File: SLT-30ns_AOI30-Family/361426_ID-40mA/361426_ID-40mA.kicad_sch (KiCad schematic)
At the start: 9 parts, among them T1 IBM_Transistor, T2 IBM_Transistor, T3 IBM_Transistor, T4 IBM_Transistor, U1 12-Pin_SLx_Can

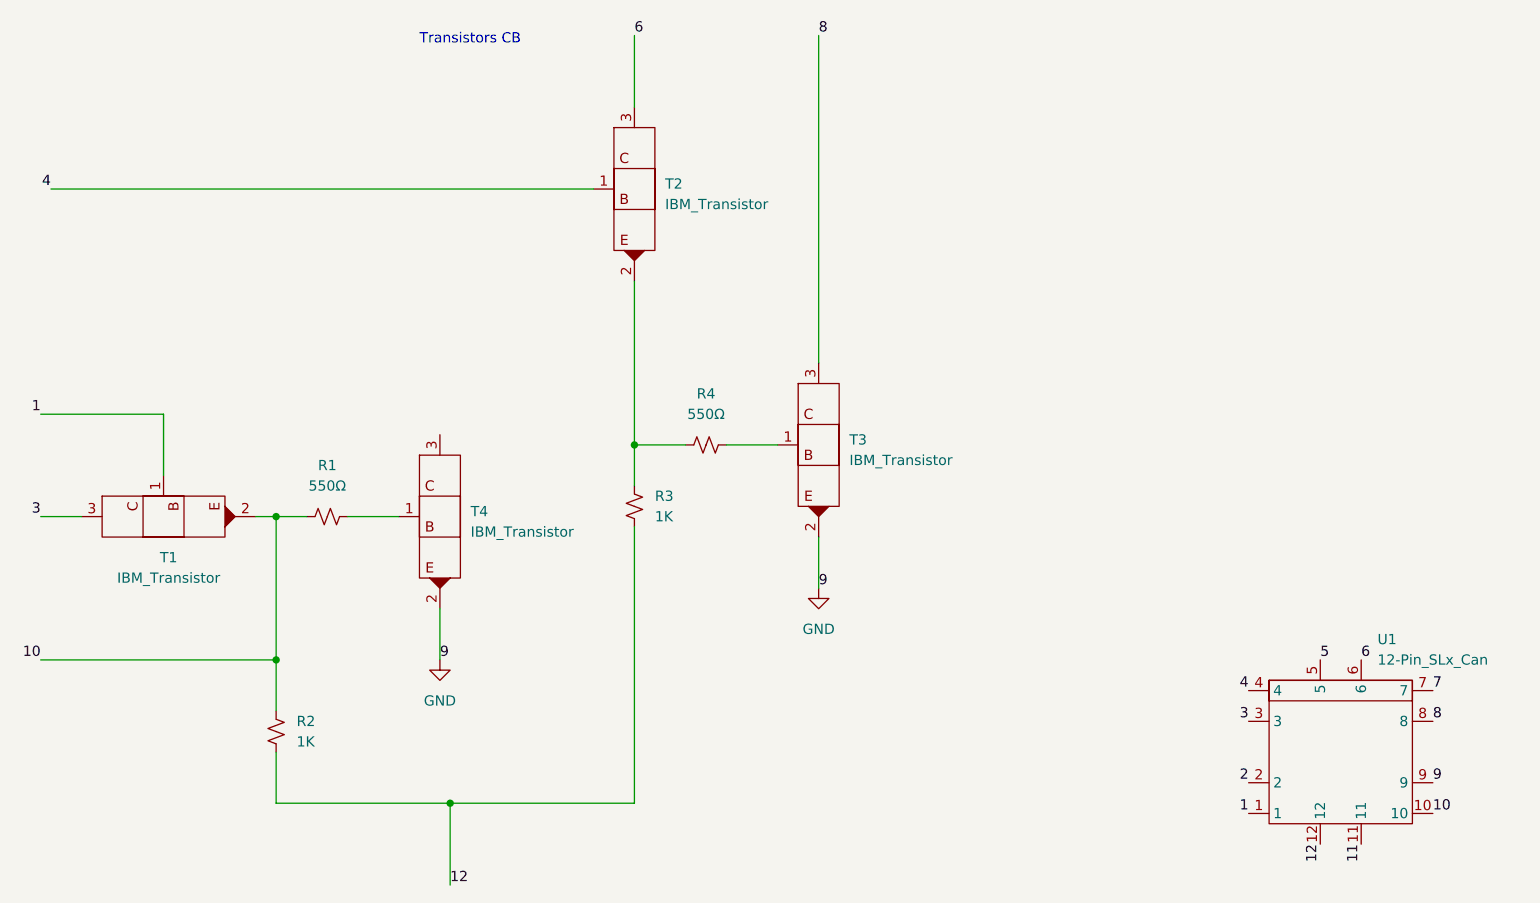
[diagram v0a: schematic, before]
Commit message: Finished off the SLT-30 family of parts, started on the SLT-700 family. Changed labeling of transistors and diodes in all schematics, but have yet to update all the pdf files. This is a TODO...
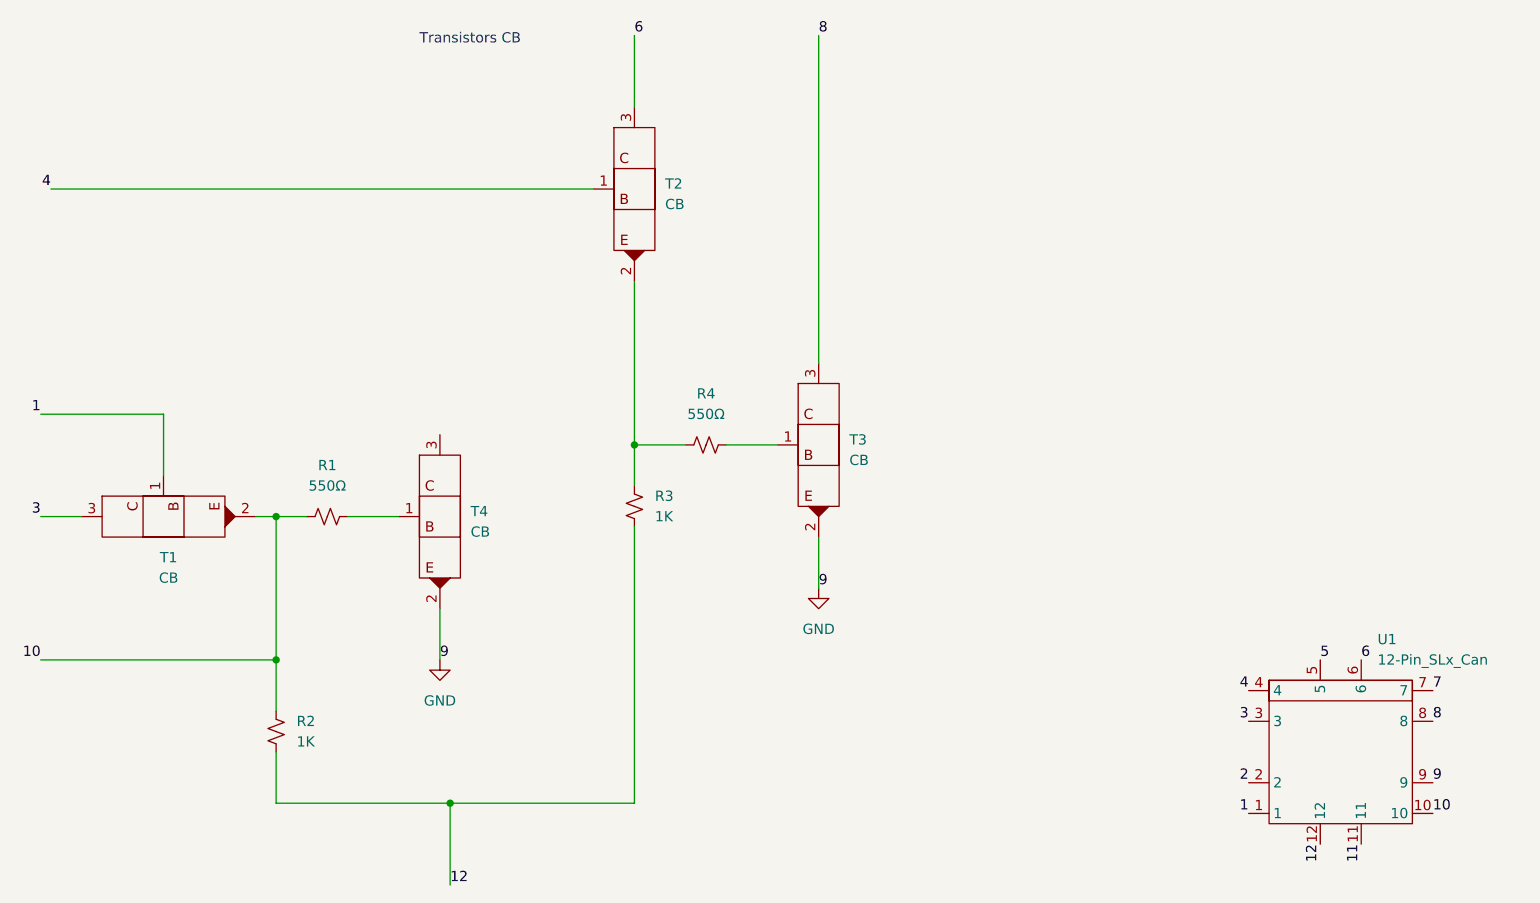
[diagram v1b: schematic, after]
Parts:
- T1, T2, T3, T4: value IBM_Transistor -> CB
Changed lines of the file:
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@@
       (effects (font (size 1.27 1.27)) (justify left))
     )
-    (property "Value" "IBM_Transistor" (id 1) (at 176.53 97.1549 0)
+    (property "Value" "CB" (id 1) (at 176.53 97.1549 0)
       (effects (font (size 1.27 1.27)) (justify left))
     )
@@
     (in_bom yes) (on_board yes) (fields_autoplaced)
     (property "Reference" "T1" (id 0) (at 92.075 109.22 90))
-    (property "Value" "IBM_Transistor" (id 1) (at 92.075 111.76 90))
+    (property "Value" "CB" (id 1) (at 92.075 111.76 90))
     (property "Footprint" "" (id 2) (at 91.44 104.14 0)
       (effects (font (size 1.27 1.27)) hide)
@@
       (effects (font (size 1.27 1.27)) (justify left))
     )
-    (property "Value" "IBM_Transistor" (id 1) (at 153.67 65.4049 0)
+    (property "Value" "CB" (id 1) (at 153.67 65.4049 0)
       (effects (font (size 1.27 1.27)) (justify left))
     )
@@
       (effects (font (size 1.27 1.27)) (justify left))
     )
-    (property "Value" "IBM_Transistor" (id 1) (at 129.54 106.0449 0)
+    (property "Value" "CB" (id 1) (at 129.54 106.0449 0)
       (effects (font (size 1.27 1.27)) (justify left))
     )
@@
     )
     (path "/3aa6e313-7972-4b5e-a4c8-3414c36a4b92"
-      (reference "T1") (unit 1) (value "IBM_Transistor") (footprint "")
+      (reference "T1") (unit 1) (value "CB") (footprint "")
     )
     (path "/7b5b5180-1101-4ee8-816f-2ee7fdf5519c"
-      (reference "T2") (unit 1) (value "IBM_Transistor") (footprint "")
+      (reference "T2") (unit 1) (value "CB") (footprint "")
     )
     (path "/328beb90-f791-4a9b-9895-c45ba1d55668"
-      (reference "T3") (unit 1) (value "IBM_Transistor") (footprint "")
+      (reference "T3") (unit 1) (value "CB") (footprint "")
     )
     (path "/89303a52-64bf-4888-9e14-5c8b27a5f300"
-      (reference "T4") (unit 1) (value "IBM_Transistor") (footprint "")
+      (reference "T4") (unit 1) (value "CB") (footprint "")
     )
     (path "/75e072b9-86c1-407b-a1c4-16b7a7044004"

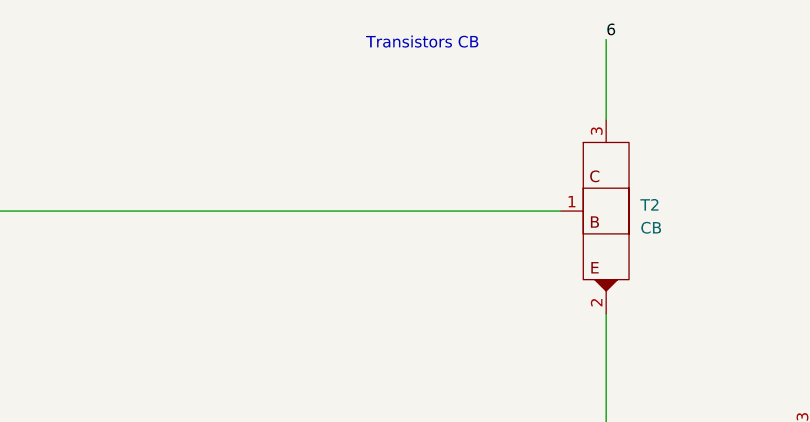
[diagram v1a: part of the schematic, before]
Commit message: Update schematic pdfs
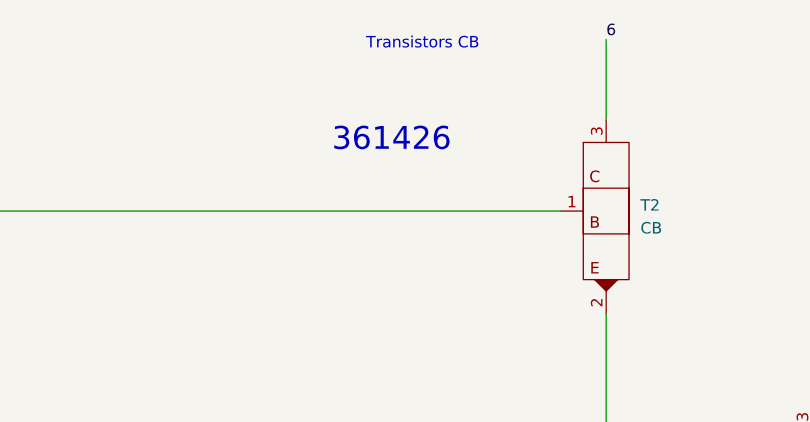
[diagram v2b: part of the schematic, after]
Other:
- note added: "361426"
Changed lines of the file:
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@@
     (stroke (width 0) (type default) (color 0 0 0 0))
+  )
+  (text "361426" (at 119.38 57.15 0)
+    (effects (font (size 2.54 2.54)) (justify left bottom))
   )
   (text "Transistors CB" (at 123.19 45.72 0)
